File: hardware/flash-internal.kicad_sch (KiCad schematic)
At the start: 24 parts, among them U3 74LVC8T245, U4 74LVC8T245, U5 74LVC8T245, U6 S29AL016J55TFIR20, U7 74LVC8T245, U8 74LVC8T245

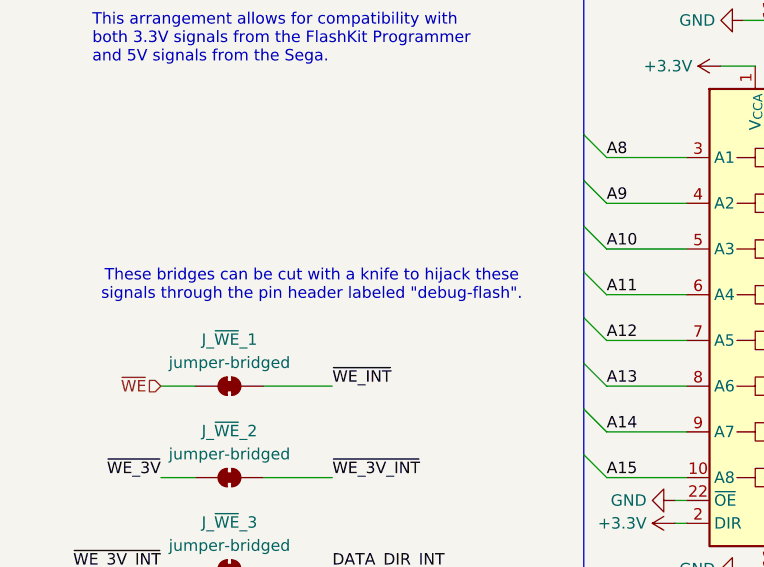
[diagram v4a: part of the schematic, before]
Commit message: Update out-of-date flash schematic comment
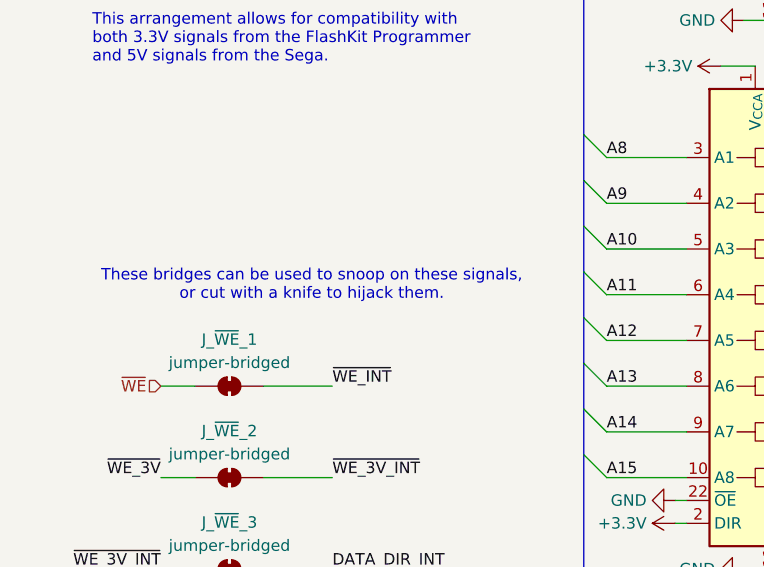
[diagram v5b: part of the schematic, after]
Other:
- note added: "These bridges can be used to snoop on these signals, or cut with a knife to hijack them."
- note removed: "These bridges can be cut with a knife to hijack these signals through the pin header labeled "debug-flash"."
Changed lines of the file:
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@@
 		)
 	)
-	(text "These bridges can be cut with a knife to hijack these\nsignals through the pin header labeled \"debug-flash\"."
+	(text "These bridges can be used to snoop on these signals,\nor cut with a knife to hijack them."
 		(exclude_from_sim no)
 		(at 40.894 100.584 0)
